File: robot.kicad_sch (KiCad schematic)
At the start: 22 parts, among them J3 Programming, J5 Switches, SW1 Reset, SW2 Action, SW3 KILL, SW4 Flash, SW6 OPTION, U1 ESP32-WROOM-32D, U8 ESP32-S3-WROOM-1

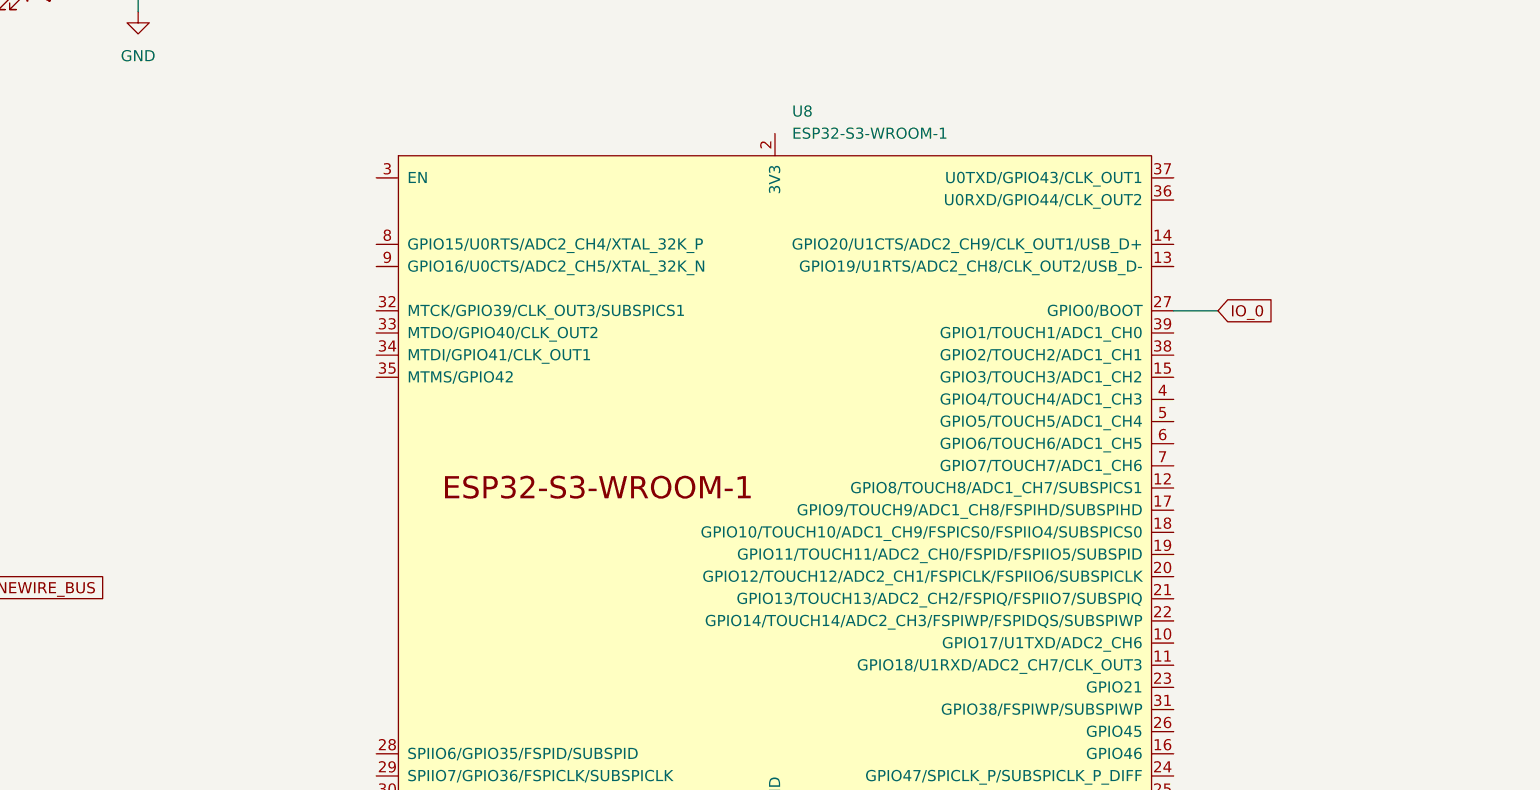
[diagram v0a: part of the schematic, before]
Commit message: started wiring up s3
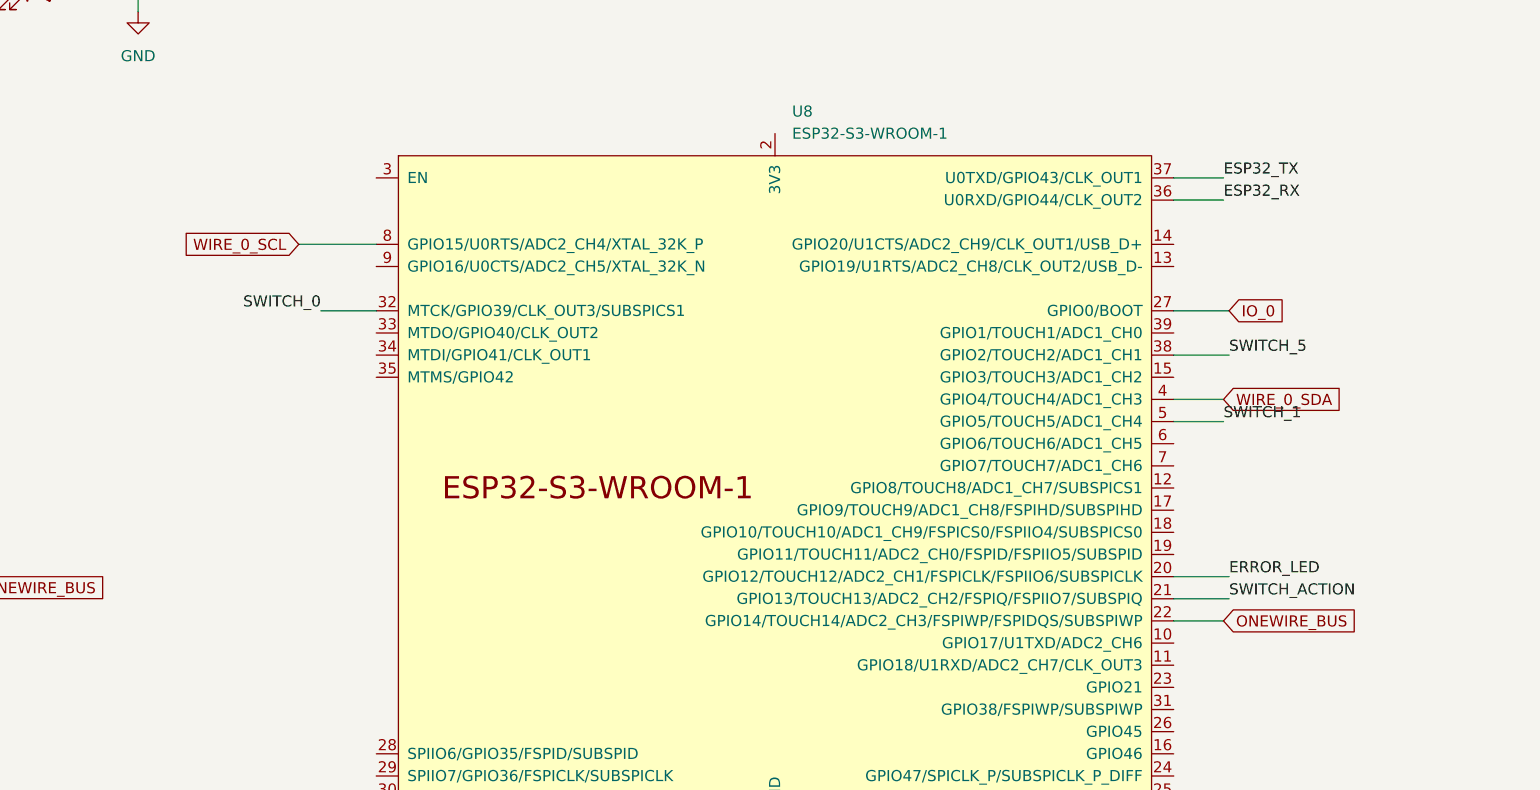
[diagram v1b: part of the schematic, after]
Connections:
- net ERROR_LED: now also U8.20 (GPIO12/TOUCH12/ADC2_CH1/FSPICLK/FSPIIO6/SUBSPICLK)
- net ESP32_RX: now also U8.36 (U0RXD/GPIO44/CLK_OUT2)
- net ESP32_TX: now also U8.37 (U0TXD/GPIO43/CLK_OUT1)
- net ONEWIRE_BUS: now also U8.22 (GPIO14/TOUCH14/ADC2_CH3/FSPIWP/FSPIDQS/SUBSPIWP)
- net SWITCH_0: now also U8.32 (MTCK/GPIO39/CLK_OUT3/SUBSPICS1)
- net SWITCH_1: now also U8.5 (GPIO5/TOUCH5/ADC1_CH4)
- net SWITCH_5: now also U8.38 (GPIO2/TOUCH2/ADC1_CH1)
- net SWITCH_ACTION: now also U8.21 (GPIO13/TOUCH13/ADC2_CH2/FSPIQ/FSPIIO7/SUBSPIQ)
- net WIRE_0_SCL: now also U8.8 (GPIO15/U0RTS/ADC2_CH4/XTAL_32K_P)
- net WIRE_0_SDA: now also U8.4 (GPIO4/TOUCH4/ADC1_CH3)
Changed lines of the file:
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@@
+    (stroke (width 0) (type default))
+  )
+  (wire (pts (xy 221.615 104.14) (xy 227.33 104.14))
+    (stroke (width 0) (type default))
+  )
+  (wire (pts (xy 121.285 83.82) (xy 130.175 83.82))
+    (stroke (width 0) (type default))
+  )
+  (wire (pts (xy 123.825 91.44) (xy 130.175 91.44))
     (stroke (width 0) (type default))
   )
@@
     (stroke (width 0) (type default))
   )
+  (wire (pts (xy 221.615 127) (xy 227.33 127))
+    (stroke (width 0) (type default))
+  )
   (wire (pts (xy 146.05 181.61) (xy 157.48 181.61))
     (stroke (width 0) (type default))
@@
     (stroke (width 0) (type default))
   )
+  (wire (pts (xy 221.615 78.74) (xy 227.33 78.74))
+    (stroke (width 0) (type default))
+  )
   (wire (pts (xy 60.96 140.97) (xy 71.12 140.97))
     (stroke (width 0) (type default))
   )
-  (wire (pts (xy 221.615 91.44) (xy 226.695 91.44))
+  (wire (pts (xy 221.615 124.46) (xy 227.965 124.46))
+    (stroke (width 0) (type default))
+  )
+  (wire (pts (xy 221.615 91.44) (xy 227.965 91.44))
     (stroke (width 0) (type default))
   )
@@
     (stroke (width 0) (type default))
   )
+  (wire (pts (xy 221.615 121.92) (xy 227.965 121.92))
+    (stroke (width 0) (type default))
+  )
   (wire (pts (xy 26.67 102.87) (xy 30.48 102.87))
     (stroke (width 0) (type default))
@@
     (stroke (width 0) (type default))
   )
+  (wire (pts (xy 221.615 96.52) (xy 227.965 96.52))
+    (stroke (width 0) (type default))
+  )
   (wire (pts (xy 92.71 156.21) (xy 95.25 156.21))
     (stroke (width 0) (type default))
@@
     (stroke (width 0) (type default))
   )
+  (wire (pts (xy 221.615 101.6) (xy 227.33 101.6))
+    (stroke (width 0) (type default))
+  )
   (wire (pts (xy 170.18 186.69) (xy 170.18 189.23))
     (stroke (width 0) (type default))
@@
     (stroke (width 0) (type default))
   )
+  (wire (pts (xy 221.615 76.2) (xy 227.33 76.2))
+    (stroke (width 0) (type default))
+  )
   (text "LED resistors between 230 and 500" (at 180.34 170.18 0)
     (effects (font (size 1.27 1.27)) (justify left bottom))
@@
     (effects (font (size 1.27 1.27)) (justify left bottom))
   )
+  (label "SWITCH_5" (at 227.965 96.52 0) (fields_autoplaced)
+    (effects (font (size 1.27 1.27)) (justify left bottom))
+  )
+  (label "SWITCH_1" (at 227.33 104.14 0) (fields_autoplaced)
+    (effects (font (size 1.27 1.27)) (justify left bottom))
+  )
   (label "ESP32_RX" (at 71.12 110.49 0) (fields_autoplaced)
     (effects (font (size 1.27 1.27)) (justify left bottom))
@@
     (effects (font (size 1.27 1.27)) (justify left bottom))
   )
+  (label "ERROR_LED" (at 227.965 121.92 0) (fields_autoplaced)
+    (effects (font (size 1.27 1.27)) (justify left bottom))
+  )
+  (label "ESP32_RX" (at 227.33 78.74 0) (fields_autoplaced)
+    (effects (font (size 1.27 1.27)) (justify left bottom))
+  )
   (label "ESP32_TX" (at 71.12 105.41 0) (fields_autoplaced)
     (effects (font (size 1.27 1.27)) (justify left bottom))
@@
     (effects (font (size 1.27 1.27)) (justify left bottom))
   )
+  (label "SWITCH_0" (at 123.825 91.44 180) (fields_autoplaced)
+    (effects (font (size 1.27 1.27)) (justify right bottom))
+  )
   (label "SWITCH_5" (at 71.12 107.95 0) (fields_autoplaced)
     (effects (font (size 1.27 1.27)) (justify left bottom))
@@
     (effects (font (size 1.27 1.27)) (justify left bottom))
   )
+  (label "ESP32_TX" (at 227.33 76.2 0) (fields_autoplaced)
+    (effects (font (size 1.27 1.27)) (justify left bottom))
+  )
   (label "SWITCH_3" (at 71.12 143.51 0) (fields_autoplaced)
     (effects (font (size 1.27 1.27)) (justify left bottom))
   )
+  (label "SWITCH_ACTION" (at 227.965 124.46 0) (fields_autoplaced)
+    (effects (font (size 1.27 1.27)) (justify left bottom))
+  )
   (label "ESP32_TX" (at 72.39 179.07 0) (fields_autoplaced)
     (effects (font (size 1.27 1.27)) (justify left bottom))
@@
     )
   )
+  (global_label "WIRE_0_SCL" (shape input) (at 121.285 83.82 180) (fields_autoplaced)
+    (effects (font (size 1.27 1.27)) (justify right))
+    (property "Intersheetrefs" "${INTERSHEET_REFS}" (at 107.7443 83.7406 0)
+      (effects (font (size 1.27 1.27)) (justify right) hide)
+    )
+  )
   (global_label "IO_36" (shape input) (at 20.32 107.95 0) (fields_autoplaced)
     (effects (font (size 1.27 1.27)) (justify left))
@@
     )
   )
-  (global_label "IO_0" (shape input) (at 226.695 91.44 0) (fields_autoplaced)
-    (effects (font (size 1.27 1.27)) (justify left))
-    (property "Intersheetrefs" "${INTERSHEET_REFS}" (at 233.2205 91.3606 0)
+  (global_label "ONEWIRE_BUS" (shape input) (at 227.33 127 0) (fields_autoplaced)
+    (effects (font (size 1.27 1.27)) (justify left))
+    (property "Intersheetrefs" "${INTERSHEET_REFS}" (at 242.806 126.9206 0)
+      (effects (font (size 1.27 1.27)) (justify left) hide)
+    )
+  )
+  (global_label "IO_0" (shape input) (at 227.965 91.44 0) (fields_autoplaced)
+    (effects (font (size 1.27 1.27)) (justify left))
+    (property "Intersheetrefs" "${INTERSHEET_REFS}" (at 234.4905 91.3606 0)
       (effects (font (size 1.27 1.27)) (justify left) hide)
     )
@@
       (effects (font (size 1.27 1.27)) (justify left) hide)
     )
+  )
+  (global_label "WIRE_0_SDA" (shape input) (at 227.33 101.6 0) (fields_autoplaced)
+    (effects (font (size 1.27 1.27)) (justify left))
+    (property "Intersheetrefs" "${INTERSHEET_REFS}" (at 240.9312 101.5206 0)
+      (effects (font (size 1.27 1.27)) (justify left) hide)
+    )

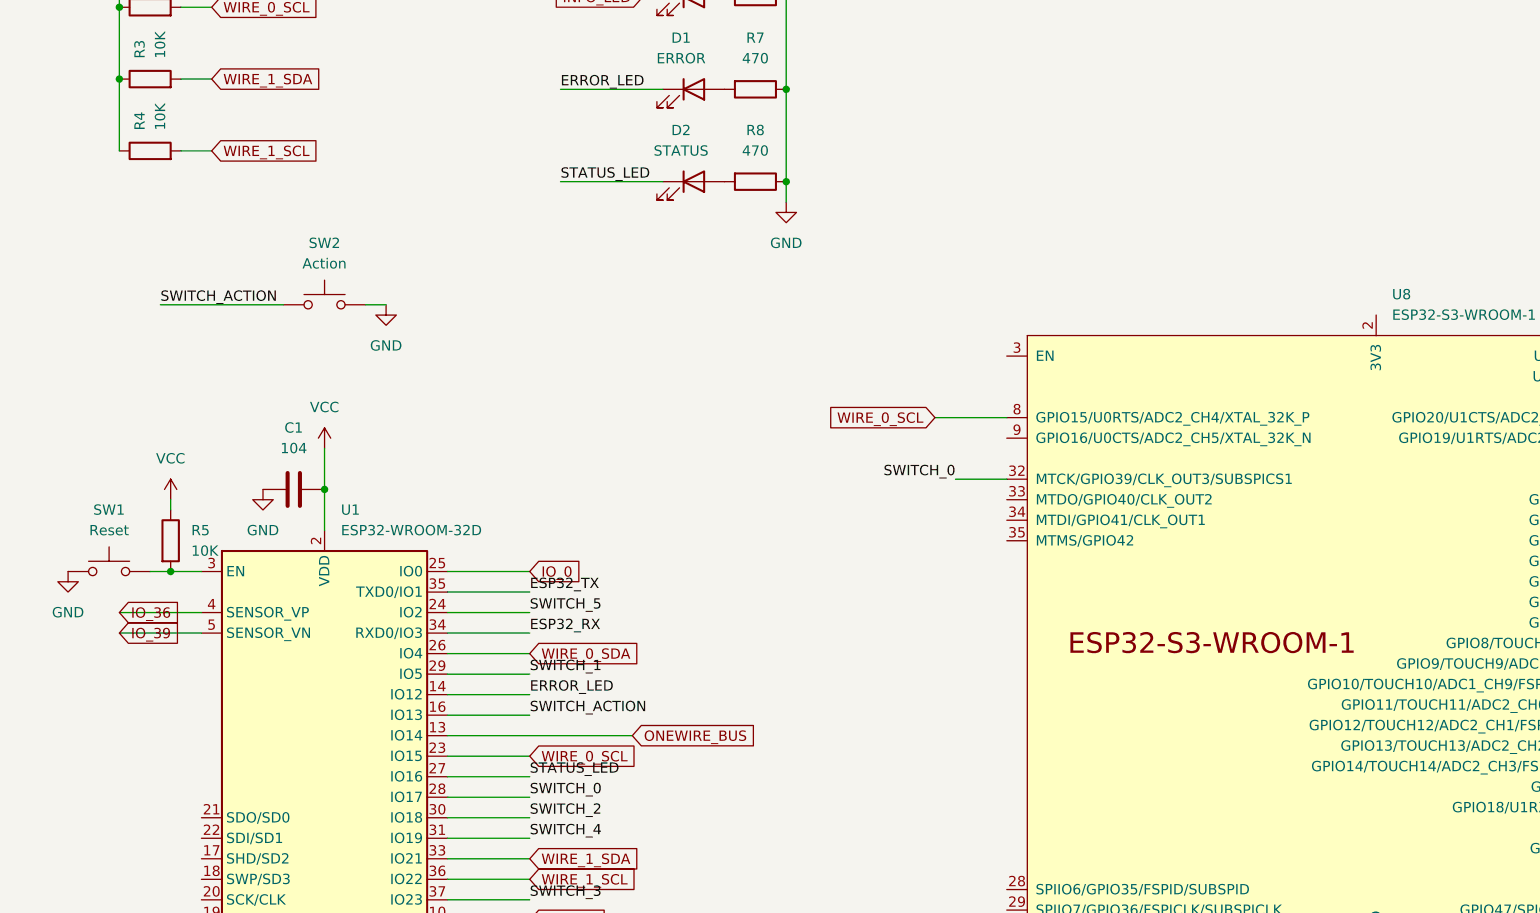
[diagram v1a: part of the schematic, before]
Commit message: Added larger filter caps + across the battery
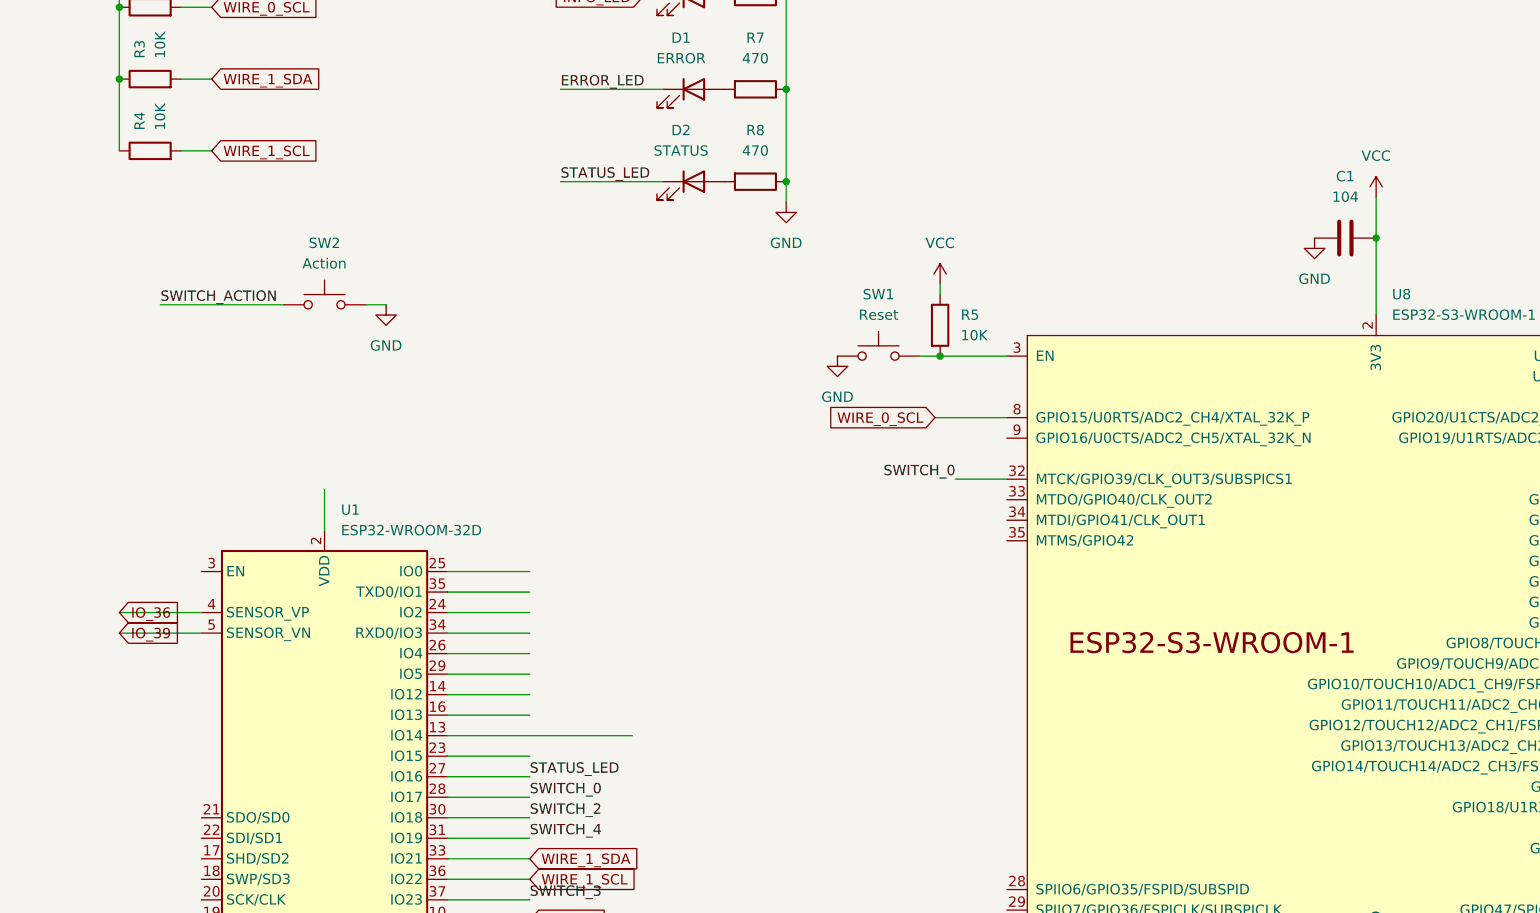
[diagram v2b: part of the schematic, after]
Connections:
- net ERROR_LED: no longer U1.14 (IO12)
- net ESP32_RX: no longer U1.34 (RXD0/IO3)
- net ESP32_TX: no longer U1.35 (TXD0/IO1)
- net IO_0: no longer U1.25 (IO0)
- net ONEWIRE_BUS: no longer U1.13 (IO14)
- net SWITCH_1: no longer U1.29 (IO5)
- net SWITCH_5: no longer U1.24 (IO2)
- net SWITCH_ACTION: no longer U1.16 (IO13)
- net VCC: now also U8.2 (3V3); no longer U1.2 (VDD)
- net WIRE_0_SCL: no longer U1.23 (IO15)
- net WIRE_0_SDA: no longer U1.26 (IO4)
- net at R5.2, SW1.2: now also U8.3 (EN); no longer U1.3 (EN)
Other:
- moved on the sheet: C1, R5, SW1
